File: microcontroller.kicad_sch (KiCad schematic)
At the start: 42 parts, among them J1 Conn_02x05_Odd_Even, J2 USB_C_Receptacle_USB2.0_16P, SW1 SKRPANE010, U1 USBLC6-2SC6, U2 STM32H563RIVx, U3 AP2112K-3.3, U4 LP5907MFX-3.3, Y1 25 MHz

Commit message: Timeline is not real
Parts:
- D1, D2, D3: value LED_Small -> LED
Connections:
- net ETH_RXER: no longer names the net of U2.39 (PD12)
- no-connect marks 25 -> 26

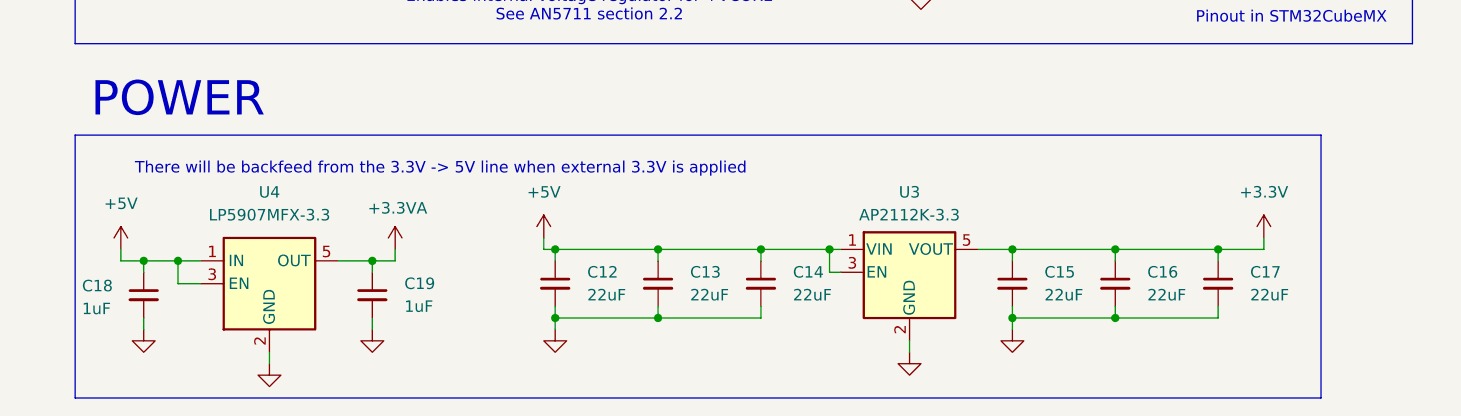
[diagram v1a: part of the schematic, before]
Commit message: Remove LP5907
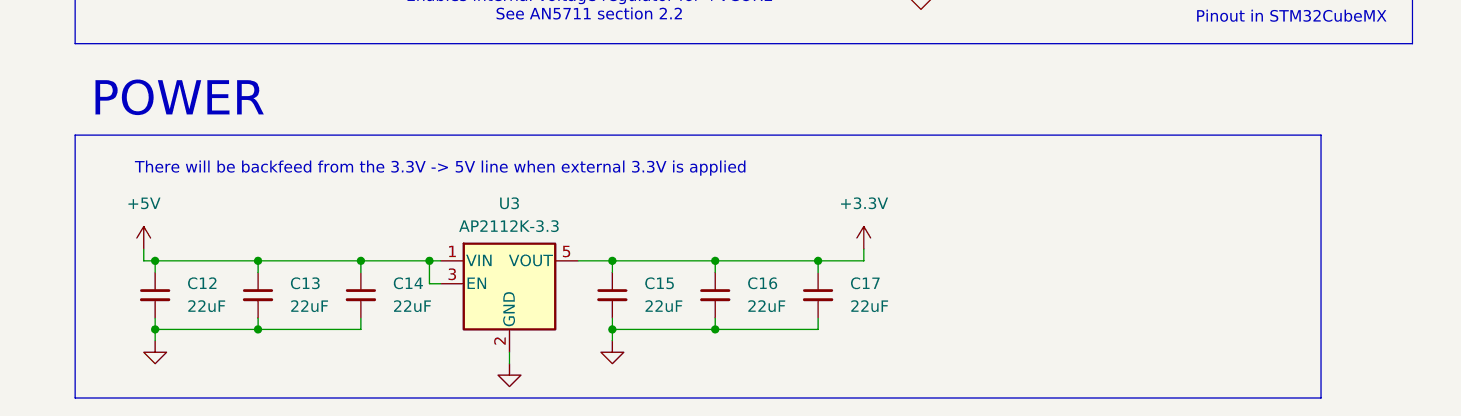
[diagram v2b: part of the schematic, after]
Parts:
- removed C18, C19: 1uF, APRLPrints:C_0603, symbol Device:C_Small
- removed U4: LP5907MFX-3.3, Package_TO_SOT_SMD:SOT-23-5, symbol Regulator_Linear:LP5907MFX-3.3
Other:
- moved on the sheet: C12, C13, C14, C15, C16, C17, U3

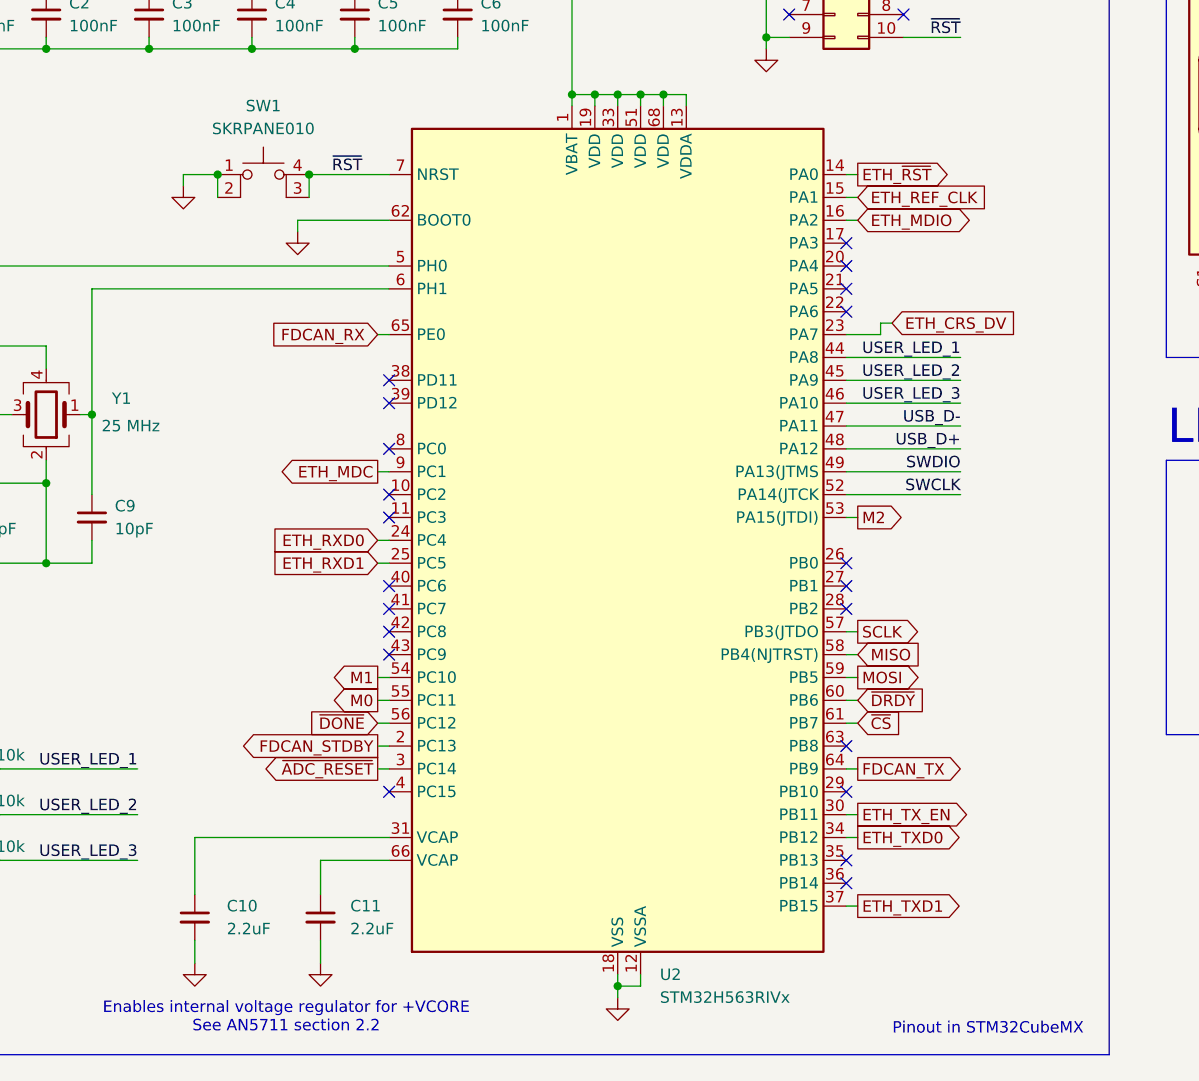
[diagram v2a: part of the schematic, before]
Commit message: Use sheet pins instead of global labels where appropriate
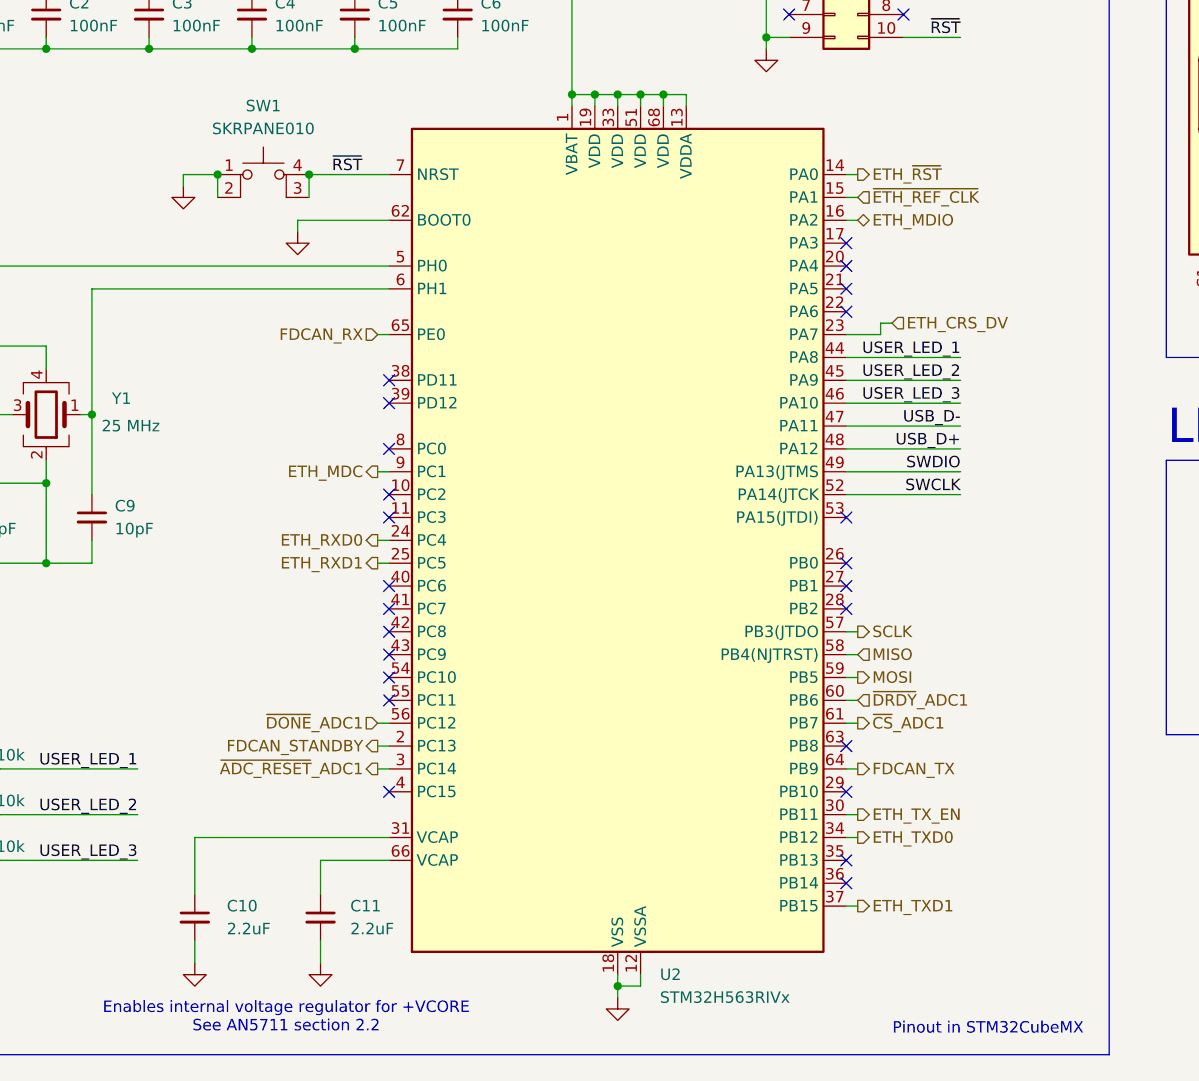
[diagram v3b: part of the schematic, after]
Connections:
- net ETH_REF_CLK renamed ~{ETH_REF_CLK}
- net FDCAN_STDBY renamed FDCAN_STANDBY
- net M0: no longer names the net of U2.55 (PC11)
- net M1: no longer names the net of U2.54 (PC10)
- net M2: no longer names the net of U2.53 (PA15(JTDI))
- net ~{ADC_RESET} renamed ~{ADC_RESET}_ADC1
- net ~{CS} renamed ~{CS}_ADC1
- net ~{DONE} renamed ~{DONE}_ADC1
- net ~{DRDY} renamed ~{DRDY}_ADC1
- no-connect marks 26 -> 29

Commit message: holy hell 2 adcs
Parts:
- added F2: 500mA, APRLPrints:Fuse_0805_2012Metric, symbol Device:Fuse_Small
- added F4: 100mA Hold, APRLPrints:Fuse_0805_2012Metric, symbol Device:Fuse_Small
- added J12: Conn_01x04, Connector_PinHeader_2.54mm:PinHeader_1x04_P2.54mm_Vertical, symbol Connector_Generic:Conn_01x04
- added J17, J3: Screw_Terminal_01x02, TerminalBlock_Phoenix:TerminalBlock_Phoenix_MPT-0,5-2-2.54_1x02_P2.54mm_Horizontal, symbol Connector:Screw_Terminal_01x02
- added J18: Conn_01x05, Connector_PinHeader_2.54mm:PinHeader_1x05_P2.54mm_Vertical, symbol Connector_Generic:Conn_01x05
- added R44, R45: 10k, APRLPrints:R_0603, symbol Device:R_Small_US
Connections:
- net +24V: now also F4.1
- net +3.3V: now also J12.3 (Pin_3), R44.1, R45.1
- net +5V: now also F2.2
- net FDCAN_STANDBY: no longer U2.2 (PC13)
- net GND: now also J2.SH (SHIELD), J12.4 (Pin_4), J17.1 (Pin_1), J3.1 (Pin_1); no longer J2.S1 (SHIELD)
- net USER_LED_1: now also U2.26 (PB0); no longer U2.44 (PA8)
- net USER_LED_2: now also U2.27 (PB1); no longer U2.45 (PA9)
- net USER_LED_3: now also U2.28 (PB2); no longer U2.46 (PA10)
- net ~{ADC_RESET}_ADC1: now also U2.2 (PC13); no longer U2.3 (PC14)
- net ~{CS}_ADC1: now also U2.56 (PC12); no longer U2.61 (PB7)
- net ~{DONE}_ADC1: now also U2.61 (PB7); no longer U2.56 (PC12)
- net ~{DRDY}_ADC2: now reaches U2.20 (PA4)
- net ~{DONE}_ADC2: now reaches U2.21 (PA5)
- net ~{ADC_RESET}_ADC2: now reaches U2.22 (PA6)
- net GPIO5: now reaches U2.38 (PD11)
- net GPIO5: now also J18.5 (Pin_5)
- net GPIO4: now reaches U2.39 (PD12)
- net GPIO4: now also J18.4 (Pin_4)
- net GPIO3: now reaches U2.40 (PC6)
- net GPIO3: now also J18.3 (Pin_3)
- net GPIO2: now reaches U2.41 (PC7)
- net GPIO2: now also J18.2 (Pin_2)
- net GPIO1: now reaches U2.42 (PC8)
- net GPIO1: now also J18.1 (Pin_1)
- net I2C_SDA: now reaches U2.43 (PC9)
- net I2C_SDA: now also J12.1 (Pin_1), R44.2
- net ~{CS}_ADC2: now reaches U2.8 (PC0)
- new net: F2.1, J3.2 (Pin_2)
- new net +24_IN: F4.2, J17.2 (Pin_2)
- new net I2C_SCL: J12.2 (Pin_2), R45.2, U2.44 (PA8)
- no-connect marks 29 -> 16
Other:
- note added: "Extra GPIO Headers"
- moved on the sheet: C12, C13, C14, C15, C16, C17, D1, D2, D3, R3, R4, R5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

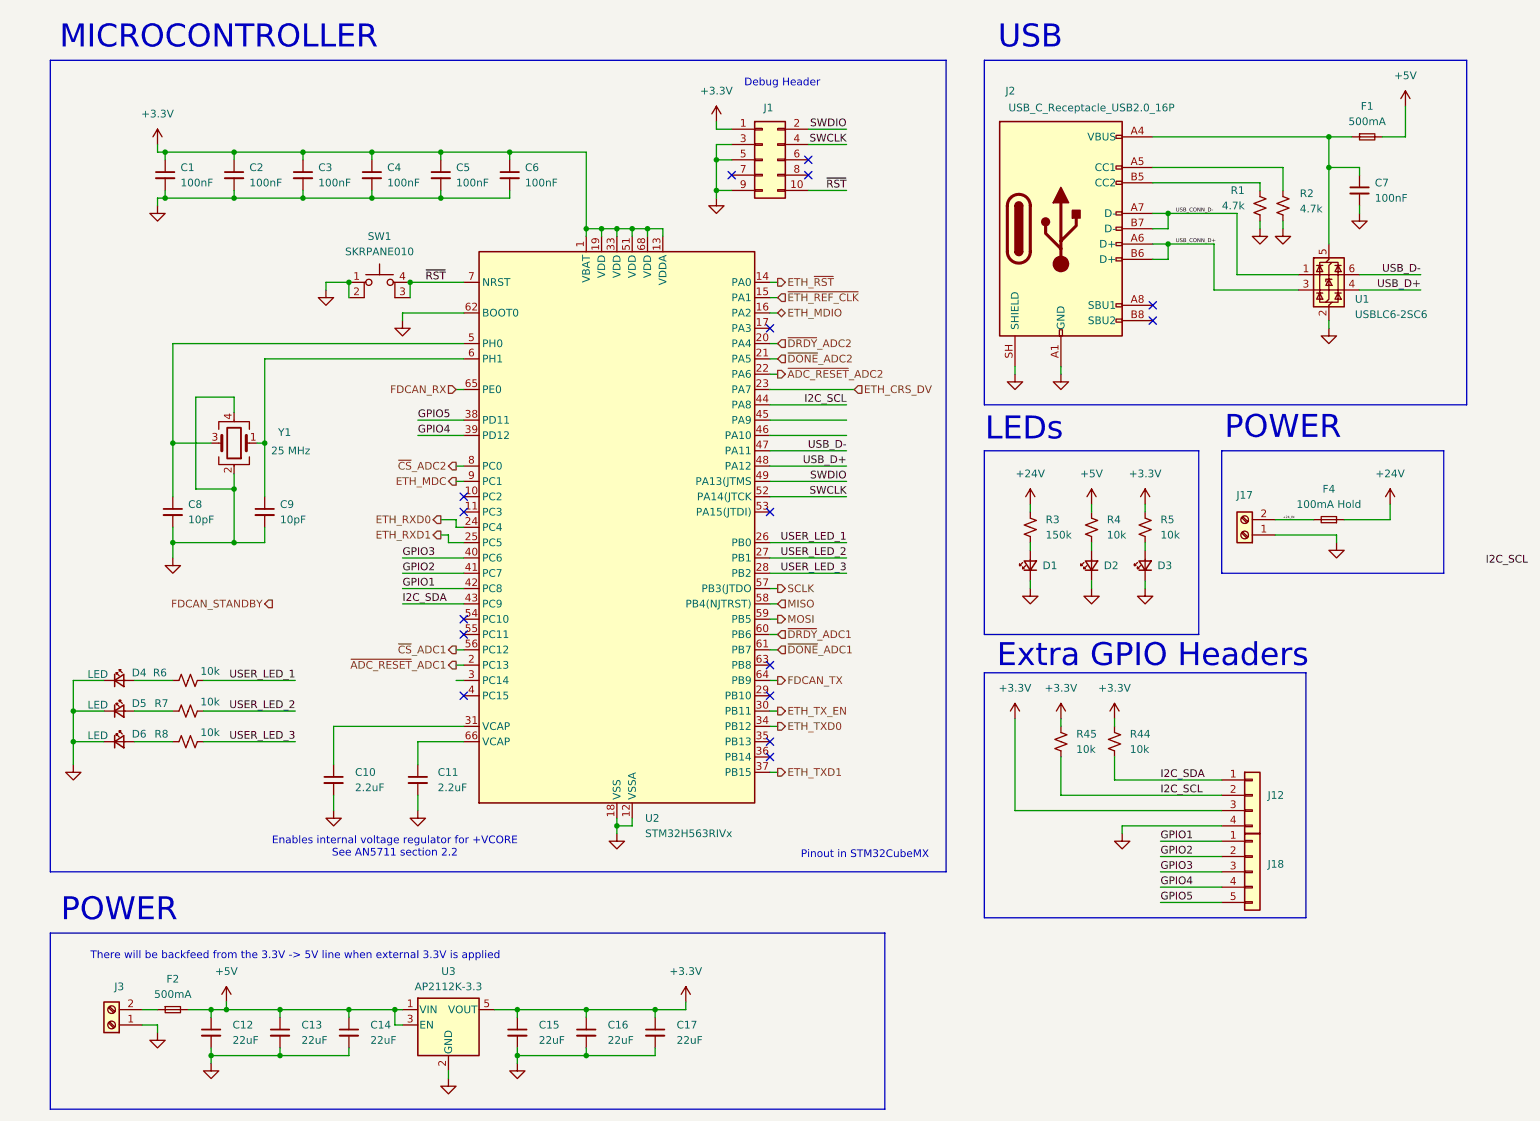
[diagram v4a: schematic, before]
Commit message: New layout just dropped (need to change silkscreen on USB and update PT.ioc)
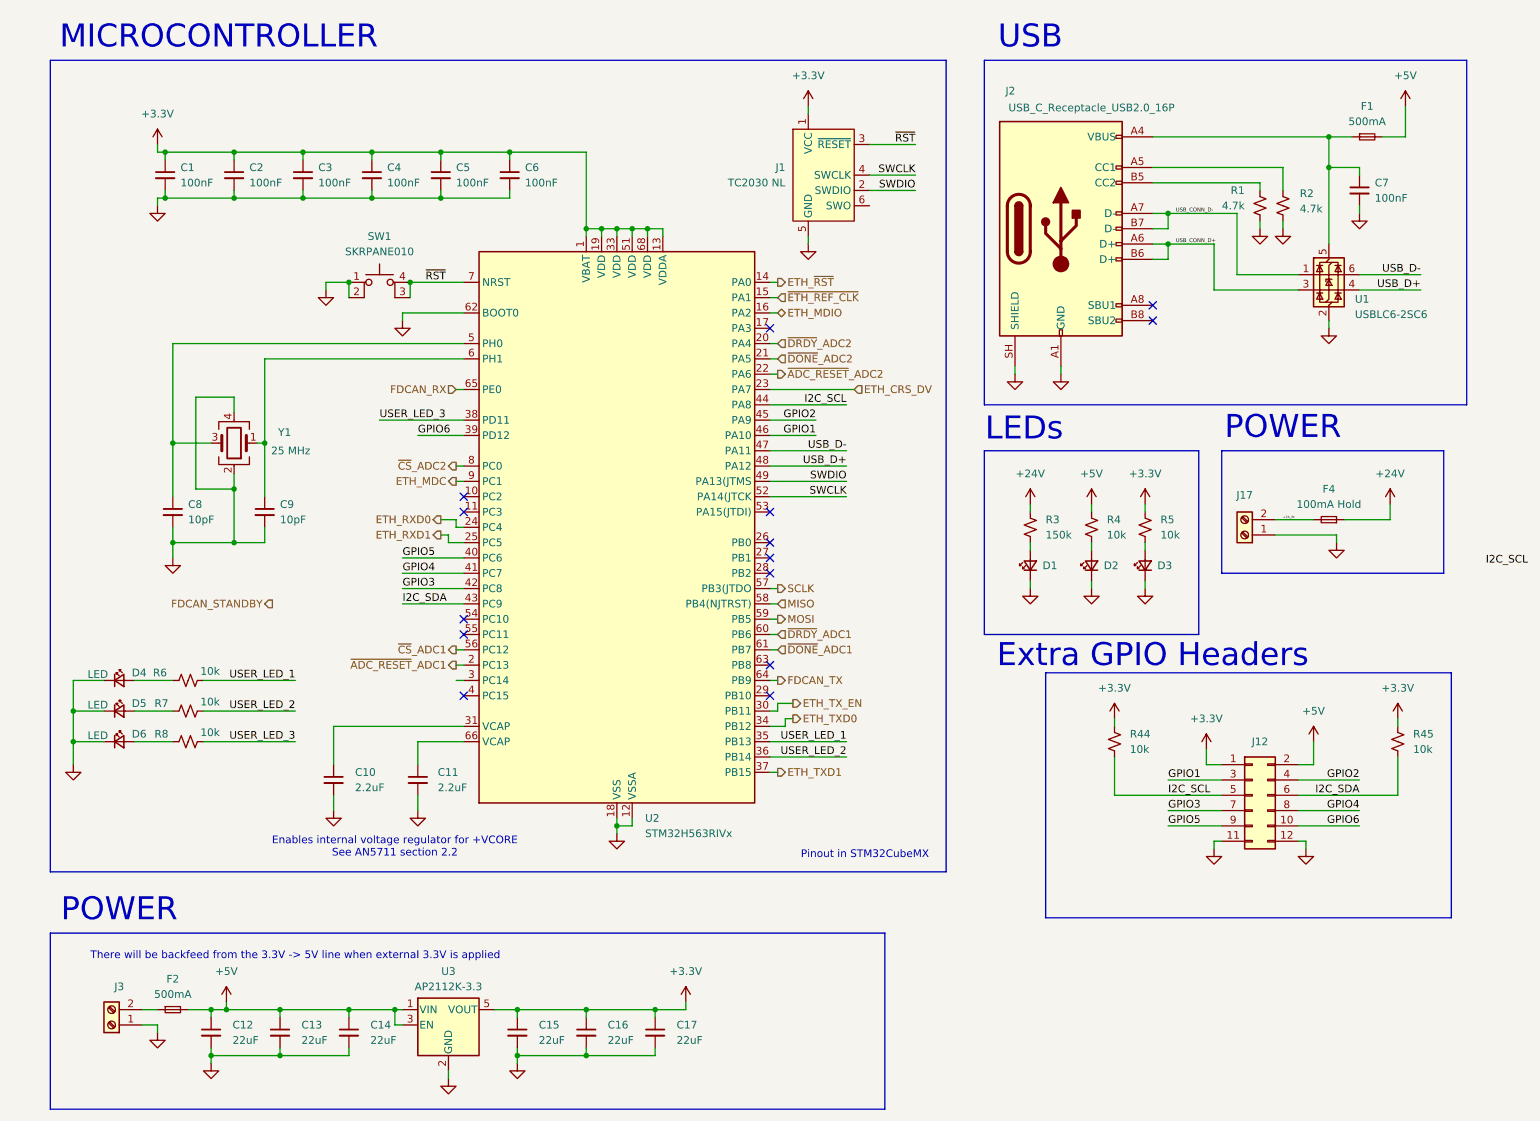
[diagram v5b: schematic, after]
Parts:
- removed J1: Conn_02x05_Odd_Even, Connector_PinHeader_2.54mm:PinHeader_2x05_P2.54mm_Vertical, symbol Connector_Generic:Conn_02x05_Odd_Even
- removed J12: Conn_01x04, Connector_PinHeader_2.54mm:PinHeader_1x04_P2.54mm_Vertical, symbol Connector_Generic:Conn_01x04
- removed J18: Conn_01x05, Connector_PinHeader_2.54mm:PinHeader_1x05_P2.54mm_Vertical, symbol Connector_Generic:Conn_01x05
- added J1: TC2030 NL, Connector:Tag-Connect_TC2030-IDC-NL_2x03_P1.27mm_Vertical, symbol Connector:Conn_ARM_SWD_TagConnect_TC2030-NL
- added J12: Conn_02x06_Top_Bottom, Connector_IDC:IDC-Header_2x06_P2.54mm_Vertical, symbol Connector_Generic:Conn_02x06_Odd_Even
- J17, J3: footprint TerminalBlock_Phoenix:TerminalBlock_Phoenix_MPT-0,5-2-2.54_1x02_P2.54mm_Horizontal -> libpt:TerminalBlock_Phoenix_MPT-0,5-2-2.54_1x02_P2.54mm_Horizontal
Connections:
- net +3.3V: now also J1.1 (VCC), J12.1 (Pin_1)
- net +5V: now also J12.2 (Pin_2)
- net GND: now also J1.5 (GND), J12.11 (Pin_11), J12.12 (Pin_12)
- net GPIO1: now also U2.46 (PA10), J12.3 (Pin_3); no longer U2.42 (PC8)
- net GPIO2: now also U2.45 (PA9), J12.4 (Pin_4); no longer U2.41 (PC7)
- net GPIO3: now also U2.42 (PC8), J12.7 (Pin_7); no longer U2.40 (PC6)
- net GPIO4: now also U2.41 (PC7), J12.8 (Pin_8); no longer U2.39 (PD12)
- net GPIO5: now also U2.40 (PC6), J12.9 (Pin_9); no longer U2.38 (PD11)
- net I2C_SCL: now also R44.2, J12.5 (Pin_5); no longer R45.2
- net I2C_SDA: now also R45.2, J12.6 (Pin_6); no longer R44.2
- net SWCLK: now also J1.4 (SWCLK)
- net SWDIO: now also J1.2 (SWDIO)
- net USER_LED_1: now also U2.35 (PB13); no longer U2.26 (PB0)
- net USER_LED_2: now also U2.36 (PB14); no longer U2.27 (PB1)
- net USER_LED_3: now also U2.38 (PD11); no longer U2.28 (PB2)
- net ~{RST}: now also J1.3 (~{RESET})
- new net GPIO6: J12.10 (Pin_10), U2.39 (PD12)
- no-connect marks 16 -> 14
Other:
- note removed: "Debug Header"
